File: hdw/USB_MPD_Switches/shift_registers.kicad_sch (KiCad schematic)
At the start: 7 parts

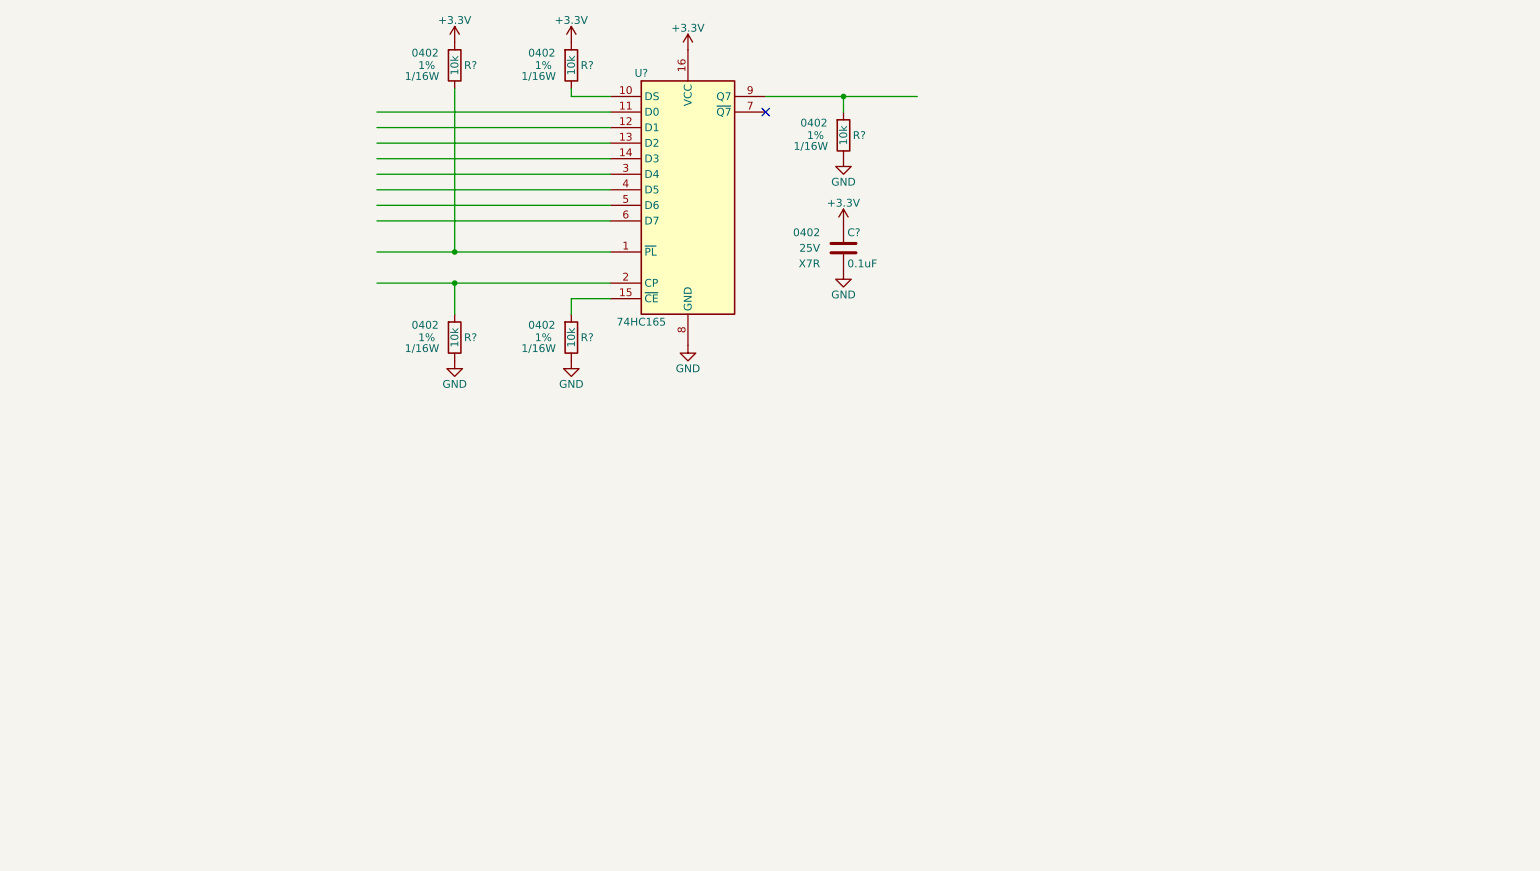
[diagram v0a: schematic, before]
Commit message: added cap touch stuff
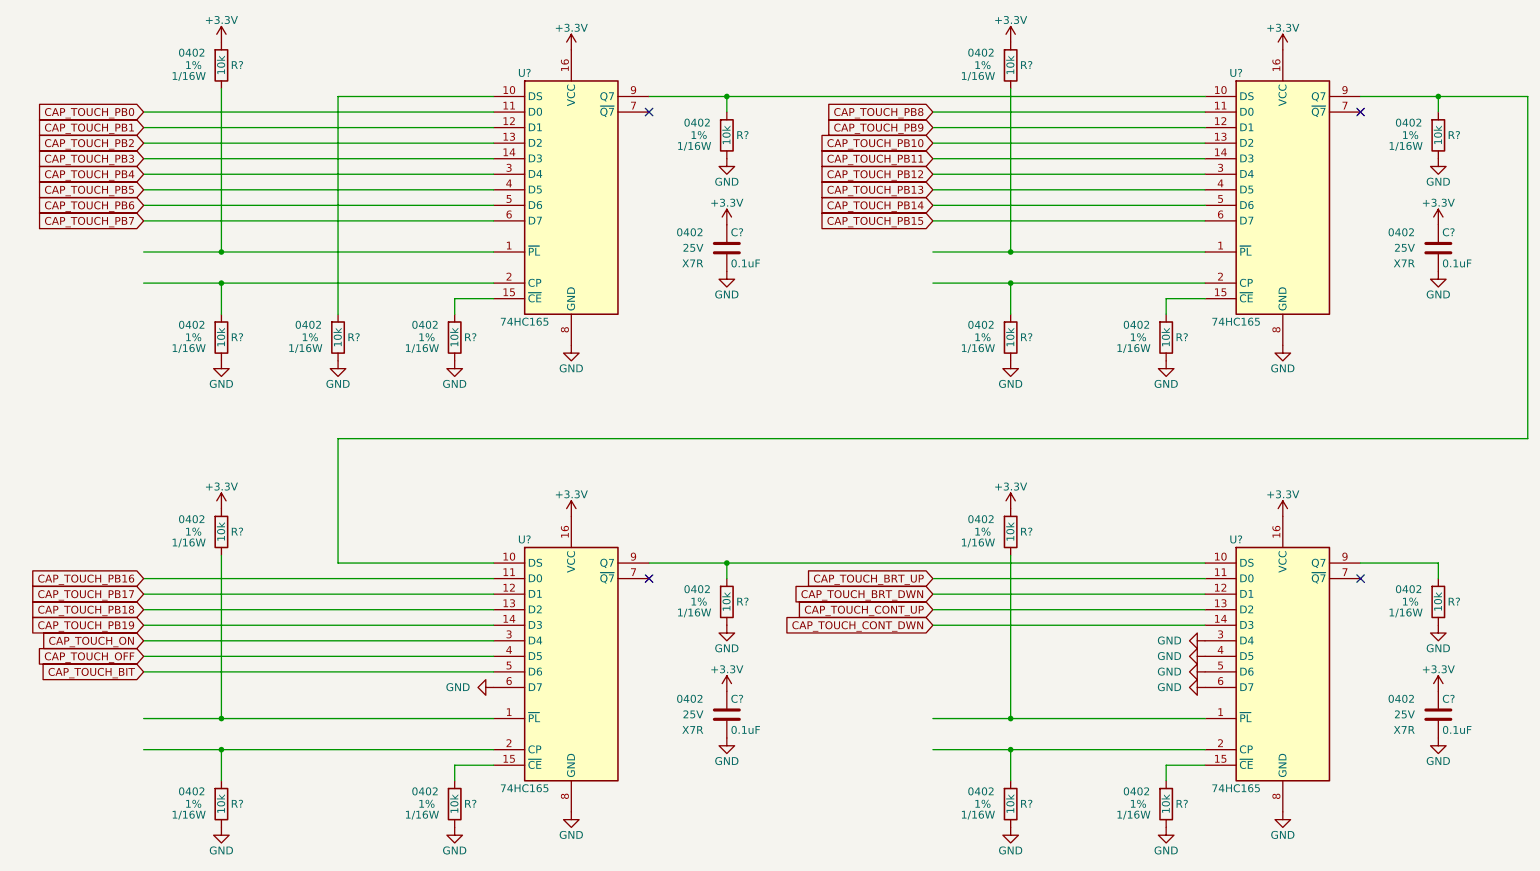
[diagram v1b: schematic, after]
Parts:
- added C? (x3): 0.1uF, symbol Custom Library:C_Custom
- added R? (x12): 10k, symbol Custom_Library:R_Custom
- added U? (x3): 74HC165, symbol 74xx:74HC165
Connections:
- net +3.3V: now also C?.1, C?.1, C?.1, R?.1, R?.1, R?.1, U?.16 (VCC), U?.16 (VCC), U?.16 (VCC); no longer R?.1
- net GND: now also R?.2, C?.2, C?.2, C?.2, R?.2, R?.2, R?.2, R?.2, R?.2, R?.2, R?.2, R?.2, R?.2, U?.3 (D4), U?.4 (D5), U?.5 (D6), U?.6 (D7), U?.6 (D7), U?.8 (GND), U?.8 (GND), U?.8 (GND)
- net at R?.1, U?.9 (Q7): now also U?.10 (DS)
- net at U?.10 (DS): now also R?.1; no longer R?.2
- net CAP_TOUCH_PB0: now reaches U?.11 (D0)
- net CAP_TOUCH_PB1: now reaches U?.12 (D1)
- net CAP_TOUCH_PB2: now reaches U?.13 (D2)
- net CAP_TOUCH_PB3: now reaches U?.14 (D3)
- net CAP_TOUCH_PB4: now reaches U?.3 (D4)
- net CAP_TOUCH_PB5: now reaches U?.4 (D5)
- net CAP_TOUCH_PB6: now reaches U?.5 (D6)
- net CAP_TOUCH_PB7: now reaches U?.6 (D7)
- new net: R?.1, U?.2 (CP) (x3)
- new net: R?.1, U?.10 (DS), U?.9 (Q7) (x2)
- new net: R?.2, U?.1 (~{PL}) (x3)
- new net: R?.1, U?.15 (~{CE}) (x3)
- new net: R?.1, U?.9 (Q7)
- new net CAP_TOUCH_BIT: U?.5 (D6)
- new net CAP_TOUCH_BRT_DWN: U?.12 (D1)
- new net CAP_TOUCH_BRT_UP: U?.11 (D0)
- new net CAP_TOUCH_CONT_DWN: U?.14 (D3)
- new net CAP_TOUCH_CONT_UP: U?.13 (D2)
- new net CAP_TOUCH_OFF: U?.4 (D5)
- new net CAP_TOUCH_ON: U?.3 (D4)
- new net CAP_TOUCH_PB10: U?.13 (D2)
- new net CAP_TOUCH_PB11: U?.14 (D3)
- new net CAP_TOUCH_PB12: U?.3 (D4)
- new net CAP_TOUCH_PB13: U?.4 (D5)
- new net CAP_TOUCH_PB14: U?.5 (D6)
- new net CAP_TOUCH_PB15: U?.6 (D7)
- new net CAP_TOUCH_PB16: U?.11 (D0)
- new net CAP_TOUCH_PB17: U?.12 (D1)
- new net CAP_TOUCH_PB18: U?.13 (D2)
- new net CAP_TOUCH_PB19: U?.14 (D3)
- new net CAP_TOUCH_PB8: U?.11 (D0)
- new net CAP_TOUCH_PB9: U?.12 (D1)
- no-connect marks 1 -> 4
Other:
- moved on the sheet: C?, R?, U?

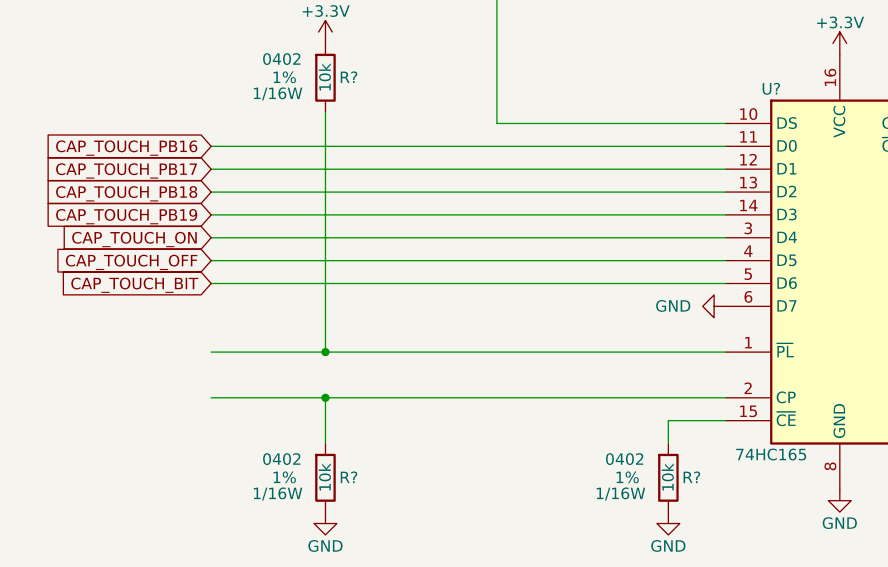
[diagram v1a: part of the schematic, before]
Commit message: added USB port, +3.3V power supply
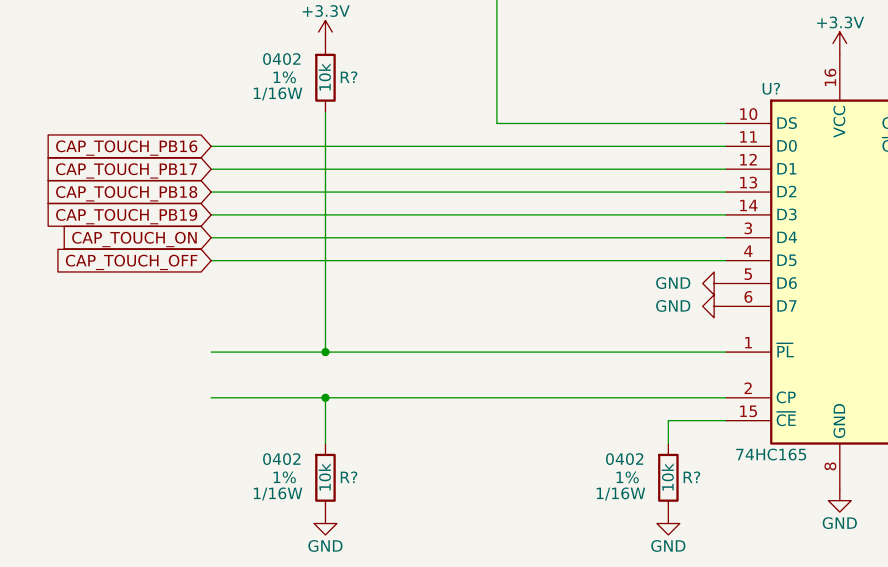
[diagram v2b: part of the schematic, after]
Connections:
- net CAP_TOUCH_BIT is gone; now on net GND: U?.5 (D6)
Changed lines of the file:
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@@
   (title_block
     (title "USB MPD")
-    (date "2024-02-01")
+    (date "2024-02-06")
     (rev "PRELIM")
     (company "Drew Maatman")
@@
     (stroke (width 0) (type default))
   )
-  (wire (pts (xy 34.925 126.365) (xy 92.075 126.365))
-    (stroke (width 0) (type default))
-  )
   (wire (pts (xy 176.53 133.985) (xy 208.28 133.985))
     (stroke (width 0) (type default))
@@
     (effects (font (size 1.27 1.27)) (justify right))
     (property "Intersheetrefs" "${INTERSHEET_REFS}" (at 16.4768 34.925 0)
-      (effects (font (size 1.27 1.27)) (justify right) hide)
-    )
-  )
-  (global_label "CAP_TOUCH_BIT" (shape input) (at 34.925 126.365 180) (fields_autoplaced)
-    (effects (font (size 1.27 1.27)) (justify right))
-    (property "Intersheetrefs" "${INTERSHEET_REFS}" (at 17.3839 126.365 0)
       (effects (font (size 1.27 1.27)) (justify right) hide)
     )
@@
         )
       )
+    )
+  )
+  (symbol (lib_id "power:GND") (at 92.075 126.365 270) (unit 1)
+    (in_bom yes) (on_board yes) (dnp no)
+    (property "Reference" "#PWR0339" (at 85.725 126.365 0)
+      (effects (font (size 1.27 1.27)) hide)
+    )
+    (property "Value" "GND" (at 88.265 126.365 90)
+      (effects (font (size 1.27 1.27)) (justify right))
+    )
+    (property "Footprint" "" (at 92.075 126.365 0)
+      (effects (font (size 1.27 1.27)) hide)
+    )
+    (property "Datasheet" "" (at 92.075 126.365 0)
+      (effects (font (size 1.27 1.27)) hide)
+    )
+    (pin "1")
+    (instances
+      (project "USB_MPD_Switches"
+        (path "/62d9a549-2742-4d98-96b6-bf7a87f3799a/c52f335e-c051-4bb5-99cb-33379bf7e677"
+          (reference "#PWR0339") (unit 1)
+        )
+      )
